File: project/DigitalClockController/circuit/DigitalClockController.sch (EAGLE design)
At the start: 20 parts, among them IC2 PIC16F886, IC3 TBD62783APG, IC4 TBD62083APG, Q1 32.768kHz, Q2 20MHz

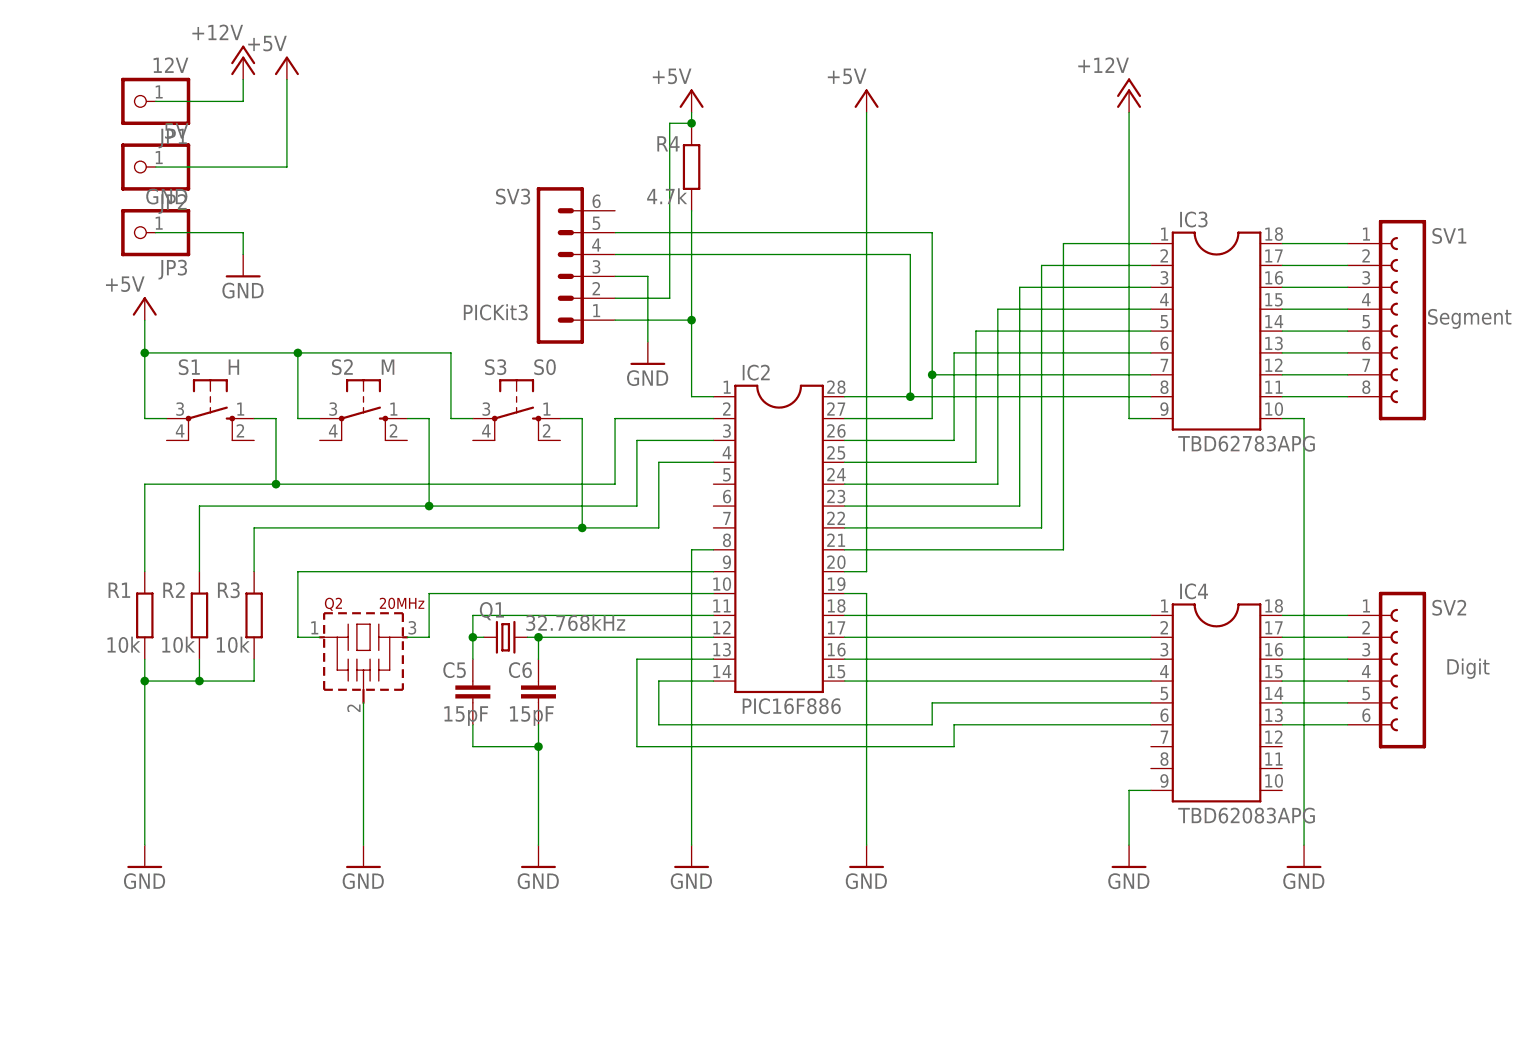
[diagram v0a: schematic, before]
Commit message: レイアウトに自由度が出るようにDisplay接続端子を増やす
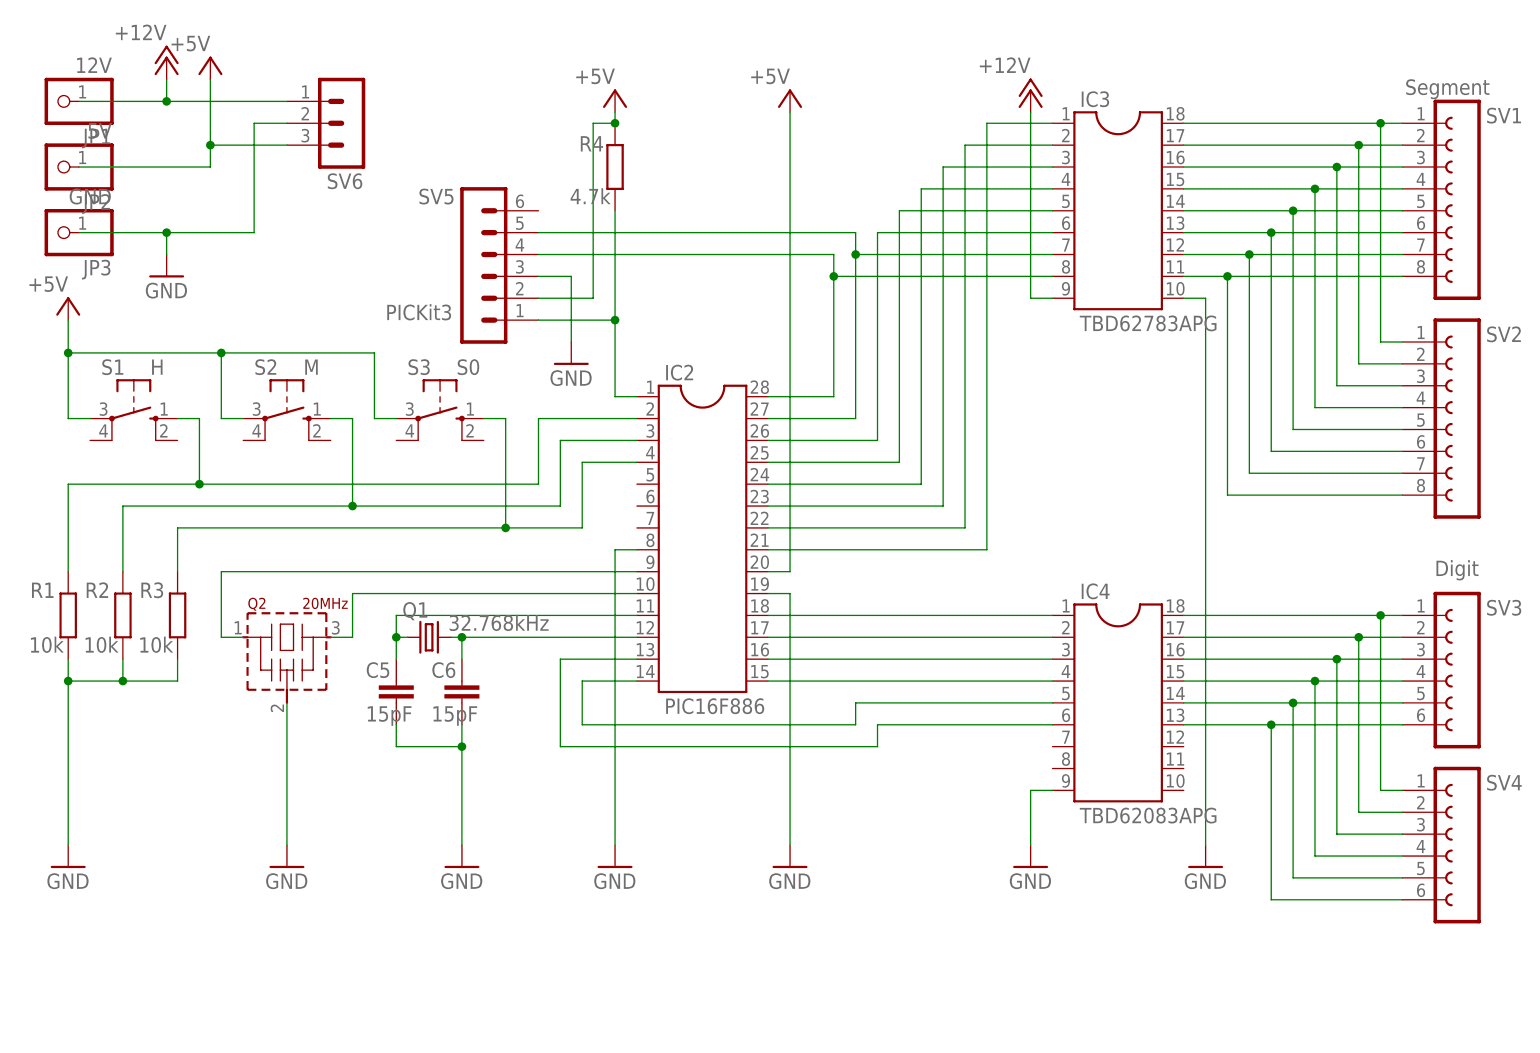
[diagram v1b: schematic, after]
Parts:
- added SV4: Digit, con-lsta:FE06-1
- added SV5: PICKit3, con-lstb:MA06-1
- added SV6: (no value), con-lstb:MA03-1
- SV2: value Digit -> Segment; device con-lsta:FE06-1 -> con-lsta:FE08-1
- SV3: value PICKit3 -> Digit; device con-lstb:MA06-1 -> con-lsta:FE06-1
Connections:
- net +12V: now also SV6.1
- net +5V: now also SV5.2, SV6.3; no longer SV3.2
- net GND: now also SV5.3, SV6.2; no longer SV3.3
- net N$10: now also SV2.2
- net N$11: now also SV2.3
- net N$12: now also SV2.4
- net N$14: now also SV5.5; no longer SV3.5
- net N$27: now also SV2.5
- net N$28: now also SV2.6
- net N$29: now also SV2.7
- net N$30: now also SV2.8
- net N$31: now also SV3.1, SV4.1; no longer SV2.1
- net N$32: now also SV3.2, SV4.2; no longer SV2.2
- net N$33: now also SV3.3, SV4.3; no longer SV2.3
- net N$34: now also SV3.4, SV4.4; no longer SV2.4
- net N$35: now also SV3.5, SV4.5; no longer SV2.5
- net N$36: now also SV3.6, SV4.6; no longer SV2.6
- net N$37: now also SV5.4; no longer SV3.4
- net N$8: now also SV5.1; no longer SV3.1
- net N$9: now also SV2.1
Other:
- moved on the sheet: C5, C6, IC2, IC3, IC4, JP1, JP2, JP3, Q1, Q2, R1, R2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

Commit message: ピン配置修正、5V-12V共通ジャンパ追加
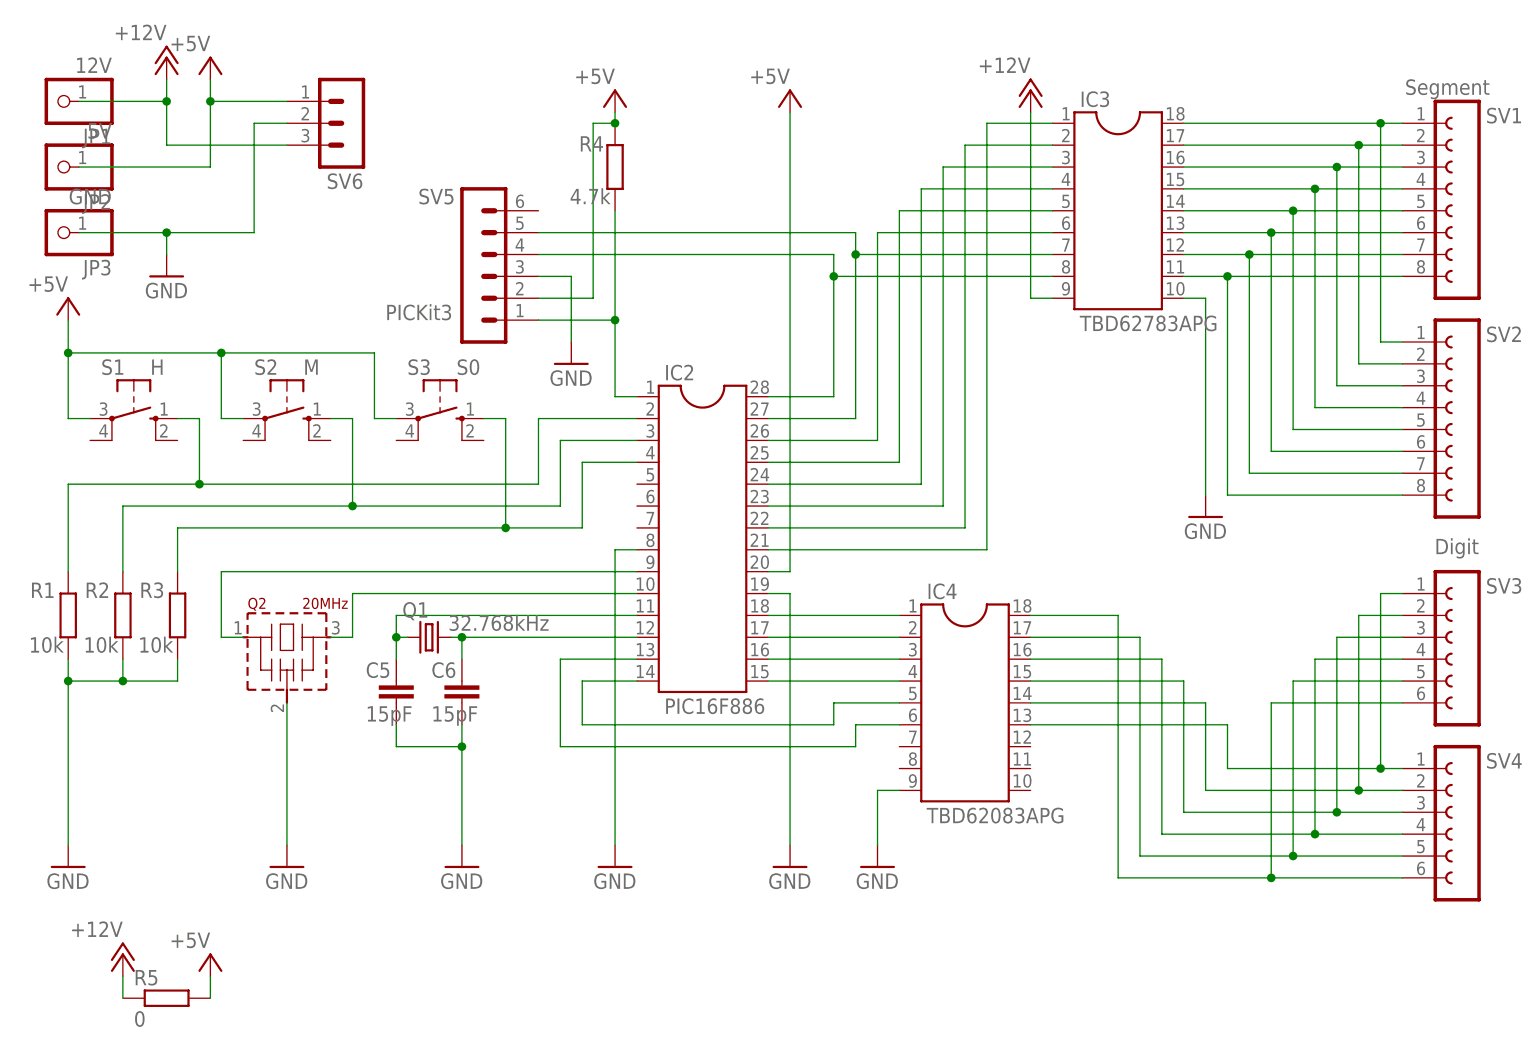
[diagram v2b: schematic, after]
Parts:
- added R5: 0, rcl:R-EU_0207/10
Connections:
- net +12V: now also R5.1, SV6.3; no longer SV6.1
- net +5V: now also R5.2, SV6.1; no longer SV6.3
- net N$31: now also IC4.13; no longer IC4.18
- net N$32: now also IC4.14; no longer IC4.17
- net N$33: now also IC4.15; no longer IC4.16
- net N$34: now also IC4.16; no longer IC4.15
- net N$35: now also IC4.17; no longer IC4.14
- net N$36: now also IC4.18; no longer IC4.13
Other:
- moved on the sheet: IC4, SV3, SV4
